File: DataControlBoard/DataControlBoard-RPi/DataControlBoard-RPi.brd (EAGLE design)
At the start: 66 x 30.5 mm, 18 parts, among them J1 USB3150-30-130-AMANUFACTURABLE, J1-L-DATA USB3150-30-130-AMANUFACTURABLE, J2 USB3150-30-130-AMANUFACTURABLE, J2-L-PWR USB3150-30-130-AMANUFACTURABLE, J3-M-DATA USB3150-30-130-AMANUFACTURABLE, J4-M-PWR USB3150-30-130-AMANUFACTURABLE, J5-S-DATA USB3150-30-130-AMANUFACTURABLE, J6-S-PWR USB3150-30-130-AMANUFACTURABLE, J7 FEMALE 2x3, J8 USB3150-30-130-AMANUFACTURABLE

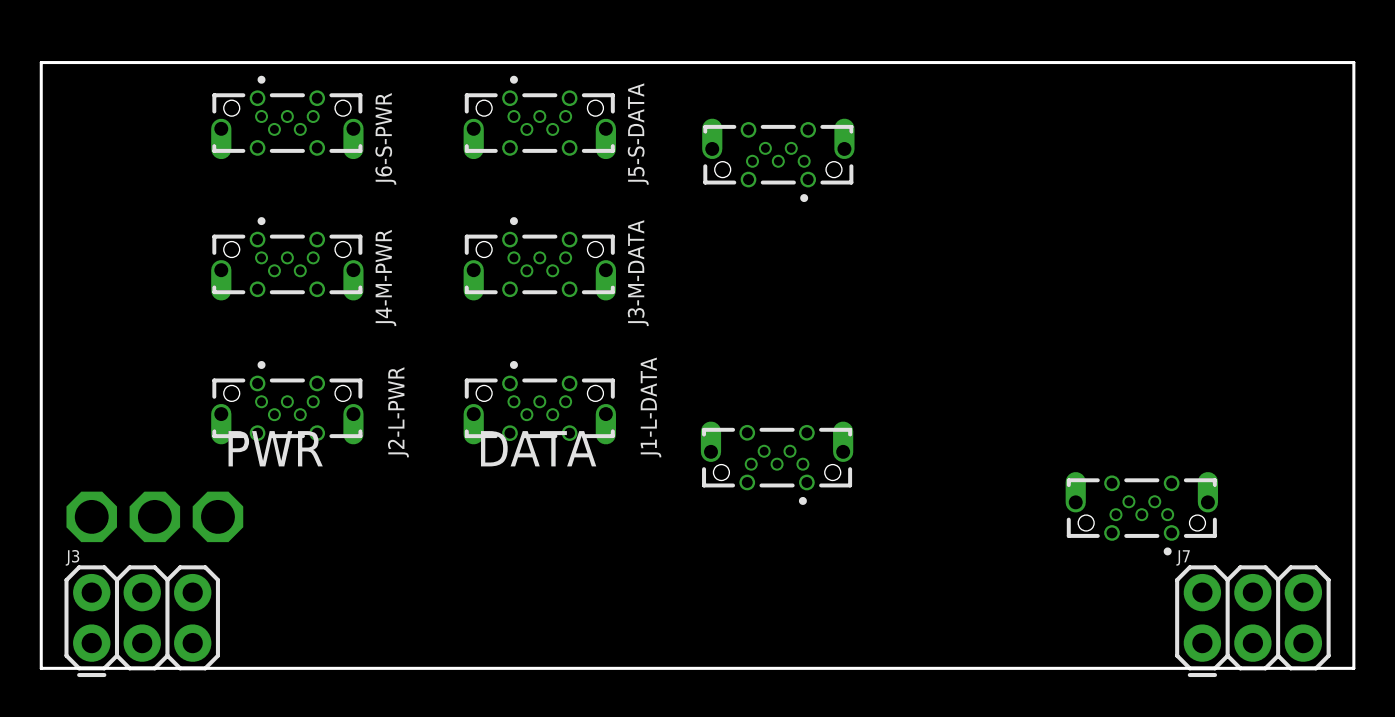
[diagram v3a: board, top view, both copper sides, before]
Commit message: Added labels. Almost ready for manufacture
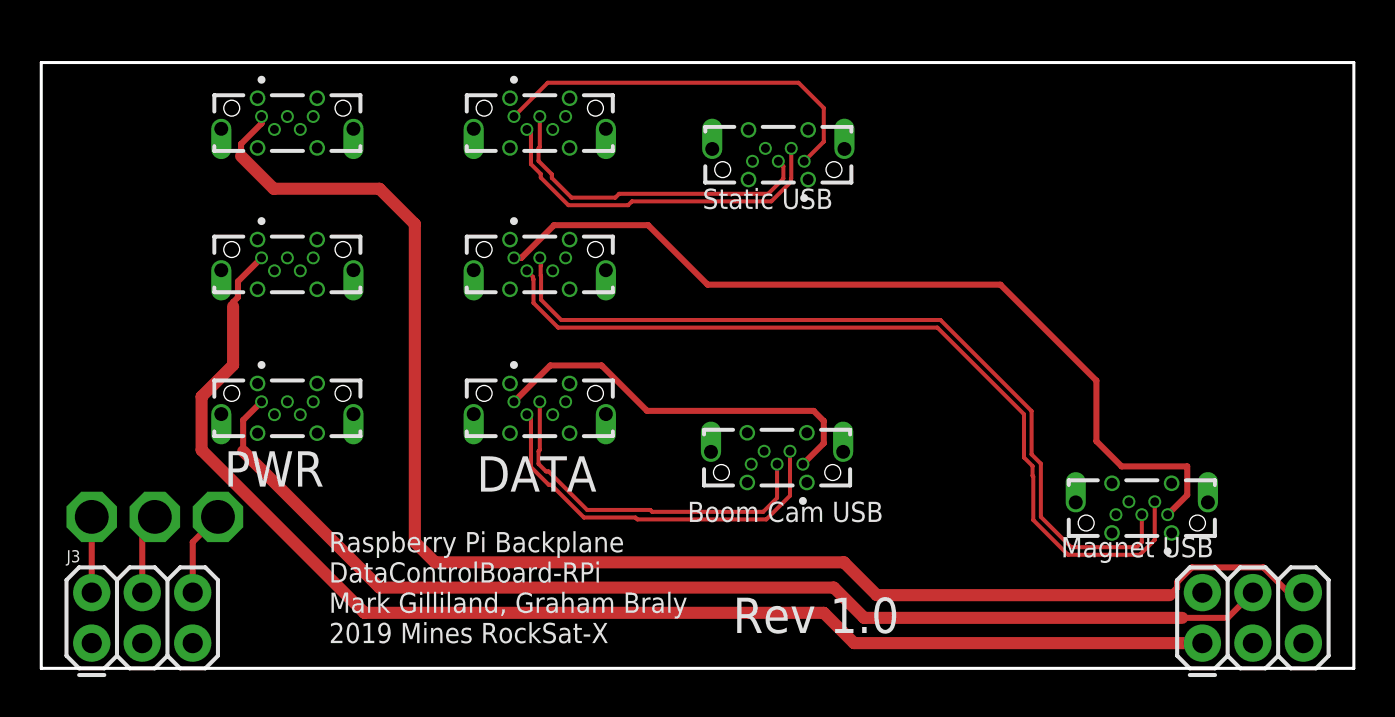
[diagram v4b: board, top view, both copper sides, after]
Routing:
- net 5V-DIG-STA: track 0.00 -> 75.7 mm
- net 5V-DIG-MAG: track 0.00 -> 65.3 mm
- net 5V-DIG-LASER: track 0.00 -> 57.7 mm
- net USB-5V-MAG: track 0.00 -> 44.2 mm
- net MAG-D_N: track 0.00 -> 43.3 mm
- net MAG-D_P: track 0.00 -> 41.9 mm
- net USB-5V-LID: track 0.00 -> 20.1 mm
- net USB-5V-STA: track 0.00 -> 19.9 mm
- net LIDAR-D_N: track 0.00 -> 19.6 mm
- net LIDAR-D_P: track 0.00 -> 18.1 mm
- net STA-D_N: track 0.00 -> 18.1 mm
- net STA-D_P: track 0.00 -> 16.8 mm
- net N$4: track 0.00 -> 4.34 mm
- net N$3: track 0.00 -> 4.07 mm
- net N$2: track 0.00 -> 3.81 mm
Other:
- board text added: "Boom Cam USB"
- board text added: "Magnet USB"
- board text added: "Raspberry Pi Backplane DataControlBoard-RPi Mark Gilliland, Graham Braly 2019 Mines RockSat-X"
- board text added: "Rev 1.0"
- board text added: "Static USB"

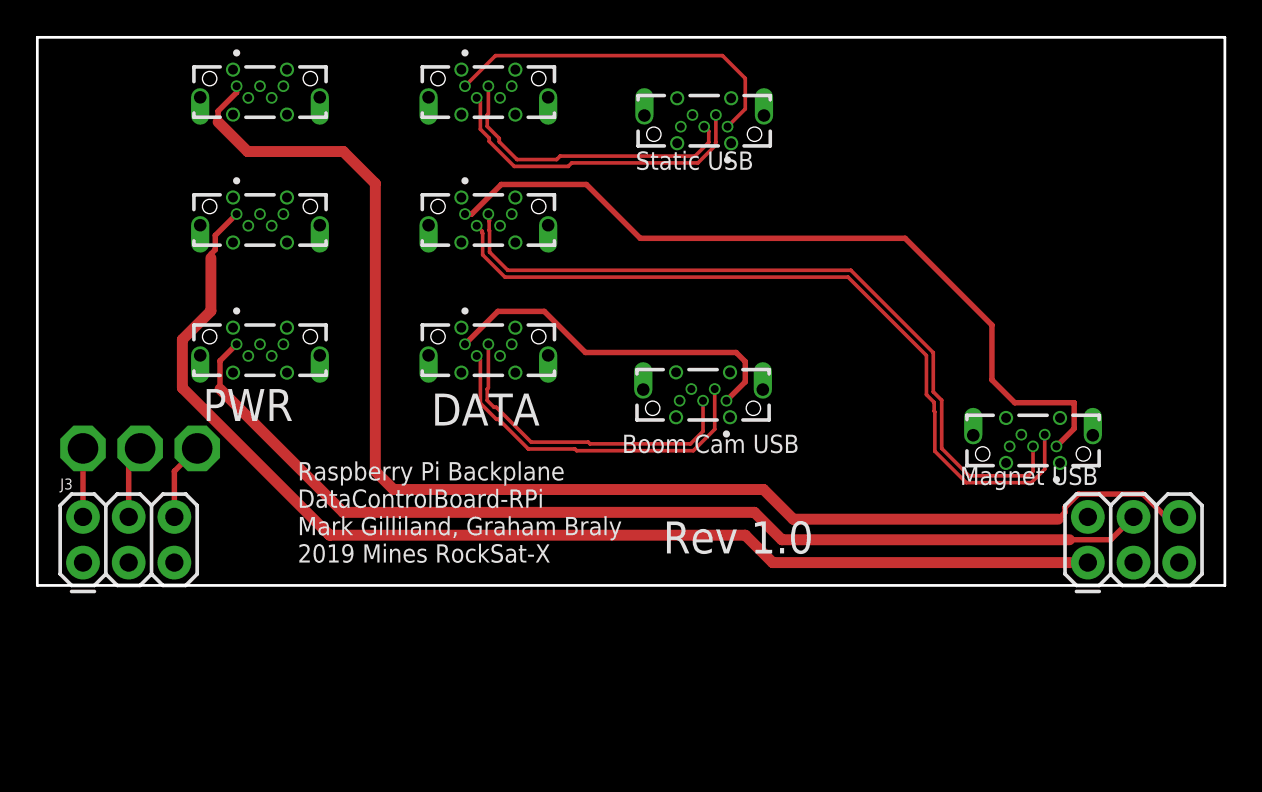
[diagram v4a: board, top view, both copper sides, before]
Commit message: Mirrored RPi components. Some traces routed
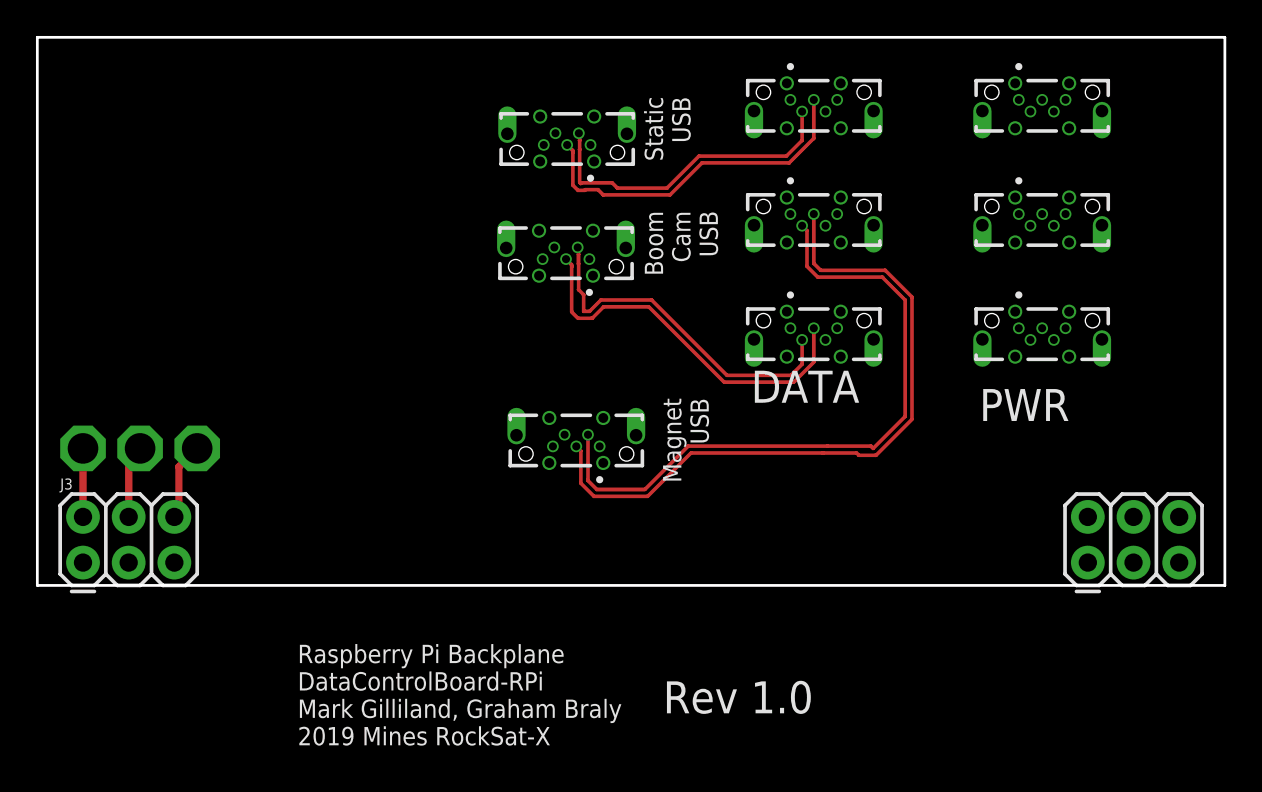
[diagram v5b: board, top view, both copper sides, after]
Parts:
- moved PH-L 63.2 mm to (2.54, 15.2), flipped to the bottom
- moved PH-S 63.2 mm to (2.54, 27.9), flipped to the bottom
- moved PH-M 63.2 mm to (2.54, 21.6), flipped to the bottom
- moved J2-L-PWR 43.5 mm to (55.9, 13.7)
- moved J6-S-PWR 43.5 mm to (55.9, 26.4)
- moved J4-M-PWR 43.5 mm to (55.9, 20.0)
- moved J1 25.4 mm to (30.0, 8.38)
- moved U$4 25.4 mm to (30.0, 6.86)
- moved J1-L-DATA 18.1 mm to (43.2, 13.7)
- moved J5-S-DATA 18.1 mm to (43.2, 26.4)
- moved J3-M-DATA 18.1 mm to (43.2, 20.0)
- moved J8 11.0 mm to (29.4, 18.8)
- moved J2 7.69 mm to (29.5, 25.1)
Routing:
- net 5V-DIG-STA: track 75.7 -> 0.00 mm
- net 5V-DIG-MAG: track 65.3 -> 0.00 mm
- net 5V-DIG-LASER: track 57.7 -> 0.00 mm
- net USB-5V-MAG: track 44.2 -> 0.00 mm
- net USB-5V-LID: track 20.1 -> 0.00 mm
- net USB-5V-STA: track 19.9 -> 0.00 mm
- net MAG-D_N: track 43.3 -> 37.3 mm
- net MAG-D_P: track 41.9 -> 38.5 mm
- net LIDAR-D_P: track 18.1 -> 21.0 mm
- net STA-D_P: track 16.8 -> 19.5 mm

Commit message: Added BOMs
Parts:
- added H1, H2, H3: MOUNT-HOLE3.0, holes:3,0
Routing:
- net MAG-D_P: track 38.5 -> 18.6 mm
- net MAG-D_N: track 37.3 -> 17.9 mm
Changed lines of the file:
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@@
 <setting verticaltext="up"/>
 </settings>
-<grid distance="10" unitdist="mil" unit="mil" style="lines" multiple="1" display="yes" altdistance="2.5" altunitdist="mil" altunit="mil"/>
+<grid distance="25" unitdist="mil" unit="mil" style="lines" multiple="1" display="yes" altdistance="2.5" altunitdist="mil" altunit="mil"/>
 <layers>
 <layer number="1" name="Top" color="4" fill="1" visible="yes" active="yes"/>
@@
 <layer number="25" name="tNames" color="7" fill="1" visible="yes" active="yes"/>
 <layer number="26" name="bNames" color="7" fill="1" visible="yes" active="yes"/>
-<layer number="27" name="tValues" color="7" fill="1" visible="yes" active="yes"/>
+<layer number="27" name="tValues" color="7" fill="1" visible="no" active="yes"/>
 <layer number="28" name="bValues" color="7" fill="1" visible="no" active="yes"/>
 <layer number="29" name="tStop" color="7" fill="3" visible="no" active="yes"/>
@@
 <text x="39.6875" y="10.16" size="1.778" layer="21">DATA</text>
 <text x="52.3875" y="9.144" size="1.778" layer="21">PWR</text>
-<text x="14.478" y="-8.89" size="1.016" layer="25">Raspberry Pi Backplane
+<text x="22.098" y="0.635" size="1.016" layer="25">Raspberry Pi Backplane
 DataControlBoard-RPi
 Mark Gilliland, Graham Braly
 2019 Mines RockSat-X</text>
-<text x="34.798" y="-7.112" size="1.778" layer="25">Rev 1.0</text>
+<text x="22.733" y="11.303" size="1.778" layer="25">Rev 1.0</text>
 <text x="33.782" y="20.828" size="1.016" layer="25" font="vector" rot="R270">Boom
 Cam
@@
 <attribute name="TP_SIGNAL_NAME" value="" x="8.89" y="7.62" size="1.778" layer="27" rot="R90" display="off"/>
 </element>
+<element name="H1" library="holes" library_urn="urn:adsk.eagle:library:237" package="3,0" package3d_urn="urn:adsk.eagle:package:14277/1" value="MOUNT-HOLE3.0" x="15.875" y="5.08" smashed="yes"/>
+<element name="H2" library="holes" library_urn="urn:adsk.eagle:library:237" package="3,0" package3d_urn="urn:adsk.eagle:package:14277/1" value="MOUNT-HOLE3.0" x="47.625" y="5.08" smashed="yes"/>
+<element name="H3" library="holes" library_urn="urn:adsk.eagle:library:237" package="3,0" package3d_urn="urn:adsk.eagle:package:14277/1" value="MOUNT-HOLE3.0" x="4.191" y="24.13" smashed="yes"/>
 </elements>
 <signals>
@@
 <wire x1="47.14781875" y1="17.526" x2="48.641" y2="16.03281875" width="0.2032" layer="1"/>
 <wire x1="43.561" y1="17.526" x2="47.14781875" y2="17.526" width="0.2032" layer="1"/>
-<wire x1="48.641" y1="9.240175" x2="48.641" y2="16.03281875" width="0.2032" layer="1"/>
 <wire x1="29.972" y1="7.732" x2="30.226" y2="7.478" width="0.2032" layer="1"/>
 <wire x1="30.226" y1="7.478" x2="30.226" y2="5.68418125" width="0.2032" layer="1"/>
 <wire x1="30.226" y1="5.68418125" x2="30.95718125" y2="4.953" width="0.2032" layer="1"/>
-<wire x1="36.352825" y1="7.366" x2="43.688" y2="7.366" width="0.2032" layer="1"/>
-<wire x1="45.680003125" y1="7.239" x2="46.639825" y2="7.239" width="0.2032" layer="1"/>
-<wire x1="45.553790625" y1="7.3652125" x2="45.680003125" y2="7.239" width="0.2032" layer="1"/>
-<wire x1="43.6887875" y1="7.3652125" x2="45.553790625" y2="7.3652125" width="0.2032" layer="1"/>
 <wire x1="43.688" y1="7.366" x2="43.6887875" y2="7.3652125" width="0.2032" layer="1"/>
 <wire x1="33.939825" y1="4.953" x2="36.352825" y2="7.366" width="0.2032" layer="1"/>
 <wire x1="30.95718125" y1="4.953" x2="33.939825" y2="4.953" width="0.2032" layer="1"/>
-<wire x1="46.639825" y1="7.239" x2="48.641" y2="9.240175" width="0.2032" layer="1"/>
+<wire x1="43.688" y1="7.366" x2="48.641" y2="16.03281875" width="0" layer="19" extent="1-1"/>
+<wire x1="36.352825" y1="7.366" x2="43.688" y2="7.366" width="0" layer="19" extent="1-1"/>
 </signal>
 <signal name="USB-5V-MAG">
@@
 <wire x1="43.40318125" y1="17.145" x2="46.99" y2="17.145" width="0.2032" layer="1"/>
 <wire x1="46.99" y1="17.145" x2="48.26" y2="15.875" width="0.2032" layer="1"/>
-<wire x1="46.482" y1="7.62" x2="48.26" y2="9.398" width="0.2032" layer="1"/>
 <wire x1="42.799" y1="19.7335" x2="42.799" y2="17.74918125" width="0.2032" layer="1"/>
-<wire x1="48.26" y1="9.398" x2="48.26" y2="15.875" width="0.2032" layer="1"/>
 <wire x1="30.622" y1="8.382" x2="30.622" y2="5.857" width="0.2032" layer="1"/>
 <wire x1="30.622" y1="5.857" x2="30.607" y2="5.842" width="0.2032" layer="1"/>
 <wire x1="30.607" y1="5.842" x2="31.115" y2="5.334" width="0.2032" layer="1"/>
-<wire x1="46.3557875" y1="7.7462125" x2="46.482" y2="7.62" width="0.2032" layer="1"/>
-<wire x1="43.9412" y1="7.7462125" x2="46.3557875" y2="7.7462125" width="0.2032" layer="1"/>
 <wire x1="43.9404125" y1="7.747" x2="43.9412" y2="7.7462125" width="0.2032" layer="1"/>
 <wire x1="33.782" y1="5.334" x2="36.195" y2="7.747" width="0.2032" layer="1"/>
-<wire x1="36.195" y1="7.747" x2="43.9404125" y2="7.747" width="0.2032" layer="1"/>
 <wire x1="31.115" y1="5.334" x2="33.782" y2="5.334" width="0.2032" layer="1"/>
+<wire x1="43.9404125" y1="7.747" x2="48.26" y2="15.875" width="0" layer="19" extent="1-1"/>
+<wire x1="36.195" y1="7.747" x2="43.9404125" y2="7.747" width="0" layer="19" extent="1-1"/>
 </signal>
 <signal name="STA-D_P" class="1">

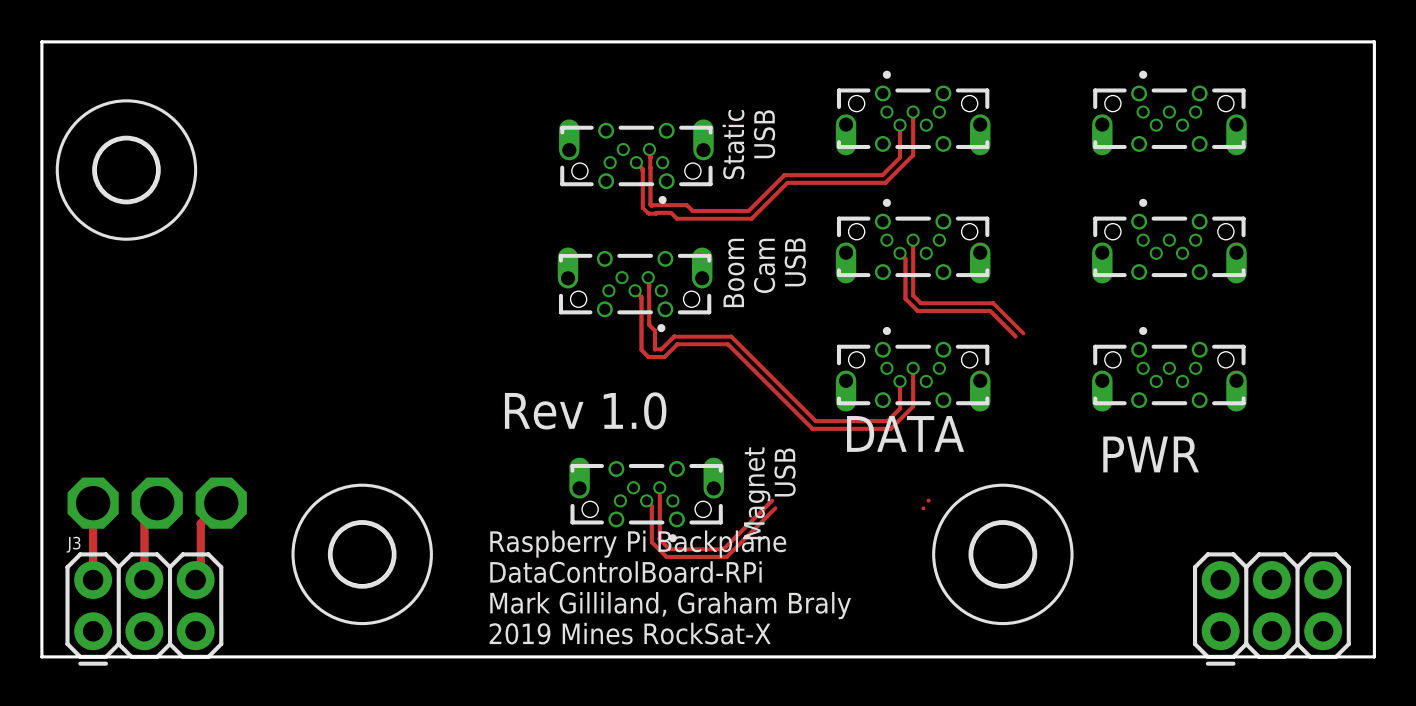
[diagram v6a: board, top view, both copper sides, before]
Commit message: Added files neccessary to manufacture
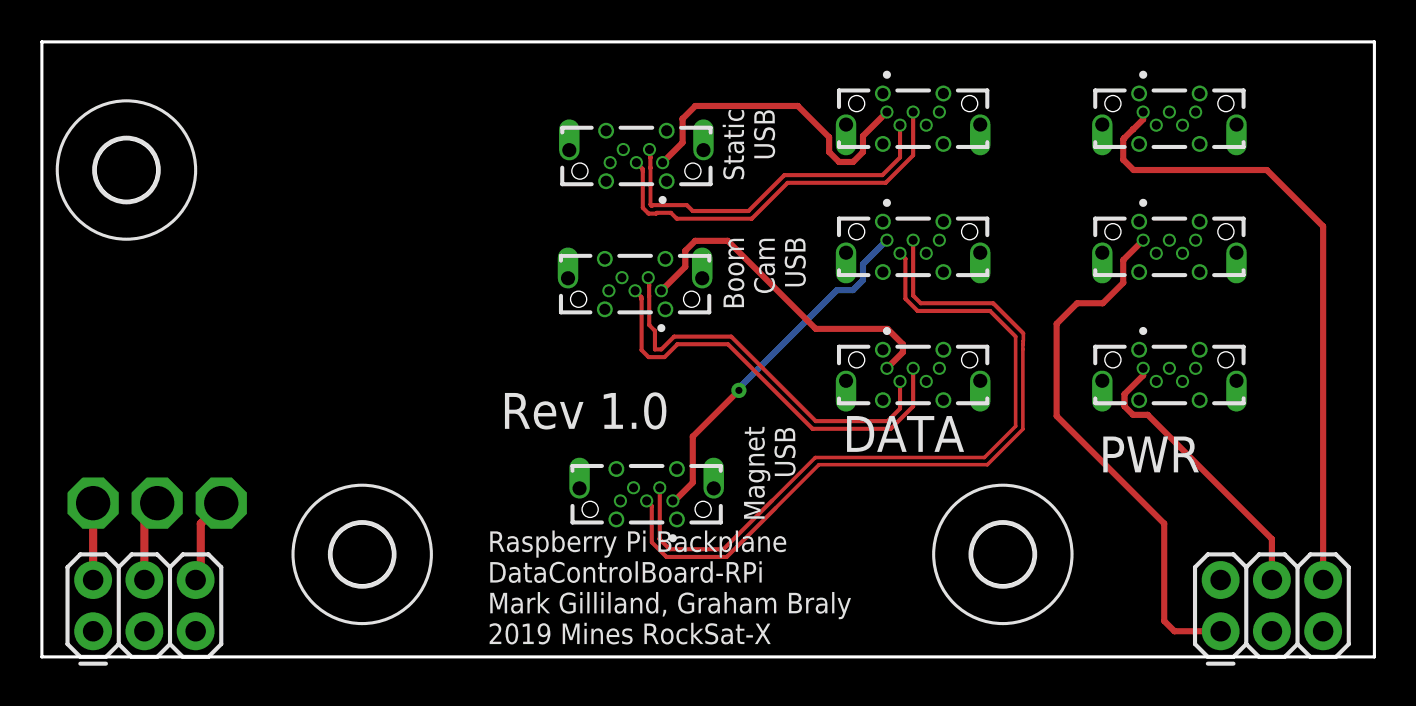
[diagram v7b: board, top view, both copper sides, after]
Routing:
- net 5V-DIG-STA: track 0.00 -> 31.6 mm
- net 5V-DIG-MAG: track 0.00 -> 26.6 mm
- net MAG-D_P: track 18.6 -> 37.2 mm
- net MAG-D_N: track 17.9 -> 36.0 mm
- net USB-5V-MAG: track 0.00 -> 17.8 mm, vias 0 -> 1
- net USB-5V-LID: track 0.00 -> 17.1 mm
- net USB-5V-STA: track 0.00 -> 16.0 mm
- net 5V-DIG-LASER: track 0.00 -> 14.3 mm
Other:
- board text added: "1 2 3"
